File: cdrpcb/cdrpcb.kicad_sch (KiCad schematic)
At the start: 41 parts, among them J1 Conn_02x04_Odd_Even, J2 Conn_01x03, J3 Conn_01x03, J4 Conn_01x03, J5 Conn_01x03, J7 Conn_01x06, J8 Conn_01x04, J9 Conn_01x03, SW1 Conn_01x02_Pin, SW2 Conn_01x02_Pin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

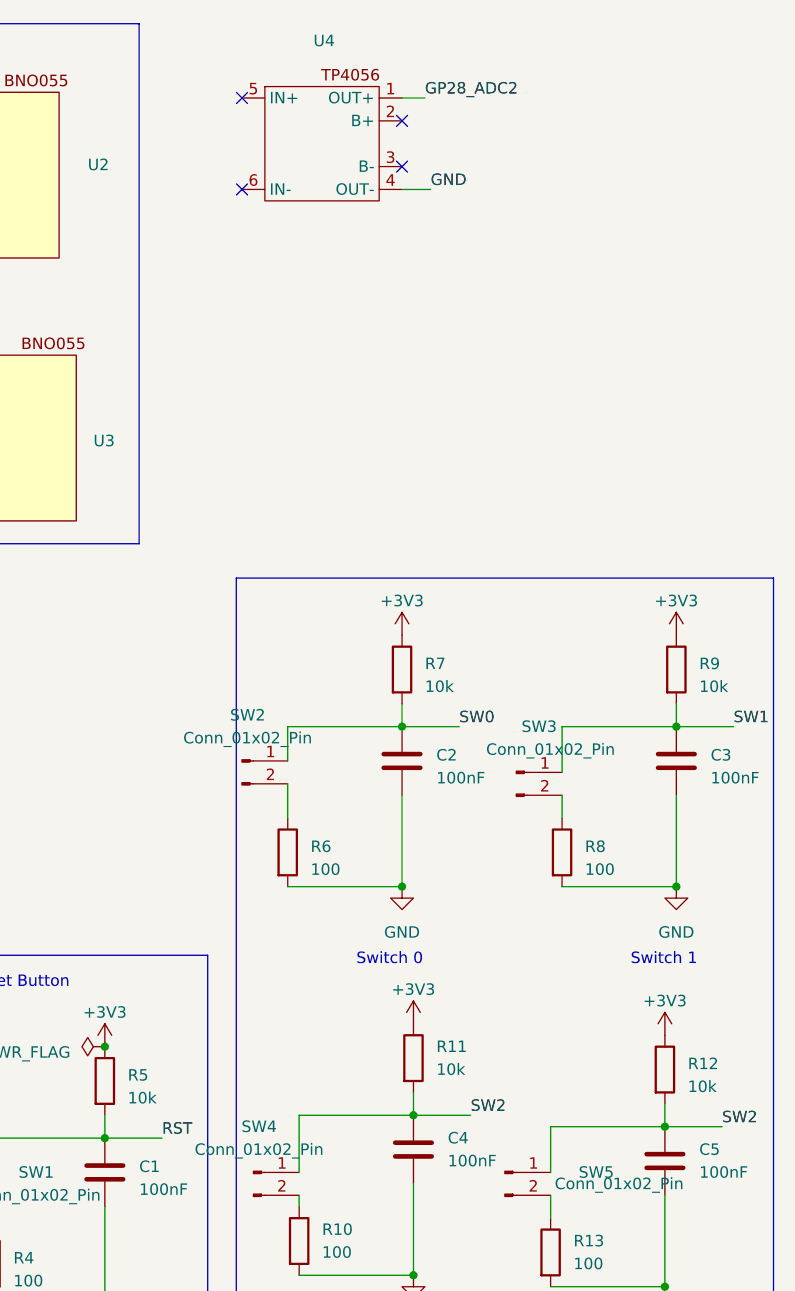
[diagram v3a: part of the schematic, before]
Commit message: add labels, fix charging circuit traces
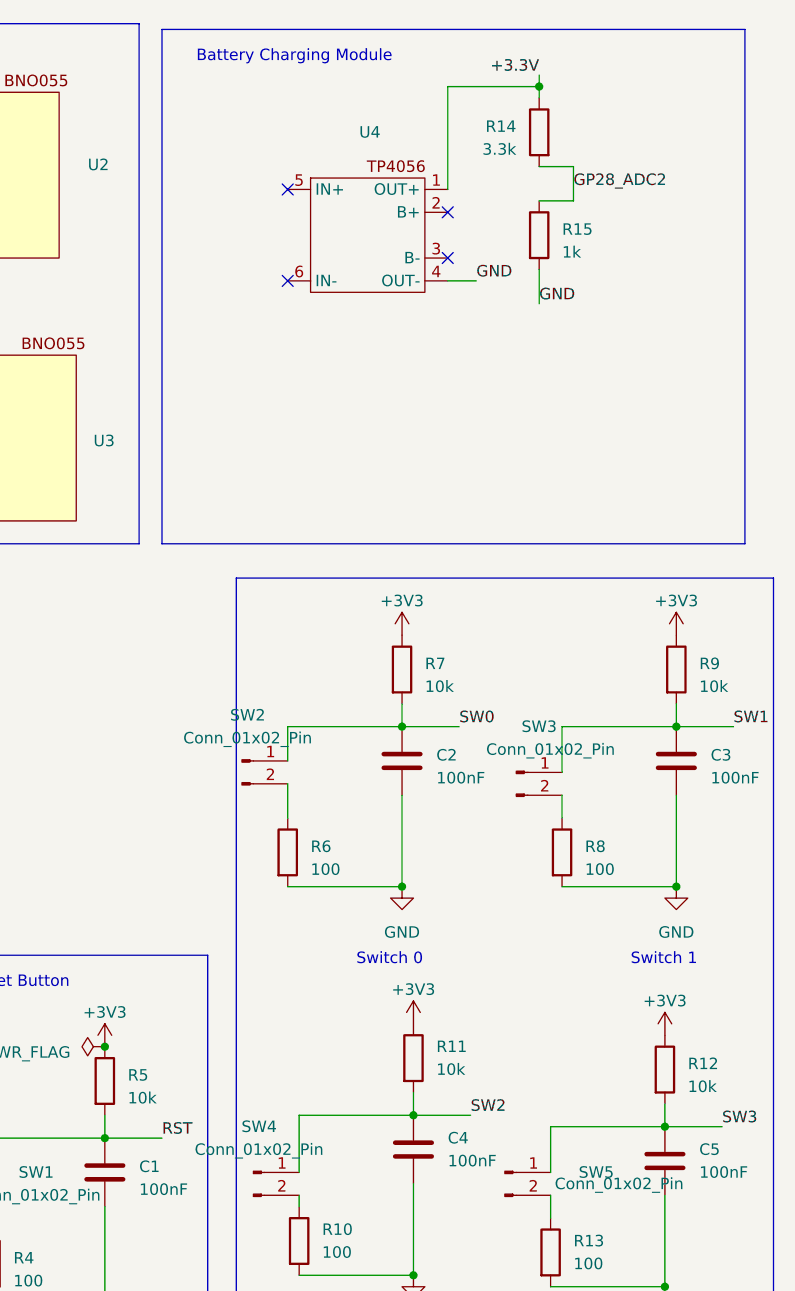
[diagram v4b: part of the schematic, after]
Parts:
- added R14: 3.3k, Resistor_THT:R_Axial_DIN0204_L3.6mm_D1.6mm_P1.90mm_Vertical, symbol Device:R
- added R15: 1k, Resistor_THT:R_Axial_DIN0204_L3.6mm_D1.6mm_P1.90mm_Vertical, symbol Device:R
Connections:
- net +3.3V: now also U4.1 (OUT+), R14.1
- net GND: now also R15.2
- net GP28_ADC2: now also R14.2, R15.1; no longer U4.1 (OUT+)
- net SW2: no longer C5.1, R12.2, SW5.1 (Pin_1)
- new net SW3: C5.1, R12.2, SW5.1 (Pin_1)
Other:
- note added: "Battery Charging Module"
- moved on the sheet: U4
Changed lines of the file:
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@@
   (junction (at 273.05 110.49) (diameter 0) (color 0 0 0 0)
   )
+  (junction (at 257.81 21.59) (diameter 0) (color 0 0 0 0)
+  )
   (no_connect (at 157.48 181.61))
-  (no_connect (at 242.57 30.48))
-  (no_connect (at 224.79 22.86))
+  (no_connect (at 247.65 40.64))
+  (no_connect (at 229.87 33.02))
   (no_connect (at 88.265 85.725))
-  (no_connect (at 242.57 25.4))
+  (no_connect (at 247.65 35.56))
   (no_connect (at 88.265 93.345))
   (no_connect (at 88.265 100.965))
   (no_connect (at 88.265 95.885))
-  (no_connect (at 224.79 33.02))
+  (no_connect (at 229.87 43.18))
   (no_connect (at 88.265 88.265))
   (no_connect (at 37.465 40.005))
@@
     (stroke (width 0) (type default))
   )
+  (wire (pts (xy 261.62 30.48) (xy 261.62 34.29))
+    (stroke (width 0) (type default))
+  )
   (wire (pts (xy 88.265 34.925) (xy 92.075 34.925))
     (stroke (width 0) (type default))
   )
-  (wire (pts (xy 242.57 33.02) (xy 245.745 33.02))
+  (wire (pts (xy 247.65 43.18) (xy 250.825 43.18))
     (stroke (width 0) (type default))
   )
@@
     (stroke (width 0) (type default))
   )
+  (wire (pts (xy 257.81 34.29) (xy 261.62 34.29))
+    (stroke (width 0) (type default))
+  )
   (wire (pts (xy 88.265 62.865) (xy 97.155 62.865))
     (stroke (width 0) (type default))
@@
     (stroke (width 0) (type default))
   )
-  (wire (pts (xy 242.57 22.86) (xy 245.11 22.86))
+  (wire (pts (xy 257.81 20.32) (xy 257.81 21.59))
     (stroke (width 0) (type default))
   )
@@
     (stroke (width 0) (type default))
   )
+  (wire (pts (xy 247.65 33.02) (xy 247.65 21.59))
+    (stroke (width 0) (type default))
+  )
   (wire (pts (xy 142.24 91.44) (xy 142.24 92.71))
     (stroke (width 0) (type default))
@@
     (stroke (width 0) (type default))
   )
+  (wire (pts (xy 247.65 21.59) (xy 257.81 21.59))
+    (stroke (width 0) (type default))
+  )
   (wire (pts (xy 31.115 57.785) (xy 37.465 57.785))
     (stroke (width 0) (type default))
@@
     (stroke (width 0) (type default))
   )
+  (wire (pts (xy 257.81 30.48) (xy 261.62 30.48))
+    (stroke (width 0) (type default))
+  )
   (wire (pts (xy 31.115 47.625) (xy 37.465 47.625))
     (stroke (width 0) (type default))
@@
     (stroke (width 0) (type default))
   )
+  (wire (pts (xy 257.81 21.59) (xy 257.81 22.86))
+    (stroke (width 0) (type default))
+  )
   (wire (pts (xy 89.535 112.395) (xy 92.075 112.395))
     (stroke (width 0) (type default))
@@
     (stroke (width 0) (type default))
   )
+  (wire (pts (xy 257.81 41.91) (xy 257.81 45.72))
+    (stroke (width 0) (type default))
+  )
   (wire (pts (xy 88.265 29.845) (xy 95.885 29.845))
     (stroke (width 0) (type default))
@@
   (wire (pts (xy 229.87 92.71) (xy 229.87 96.52))
     (stroke (width 0) (type default))
+  )
+  (rectangle (start 215.9 15.24) (end 280.67 72.39)
+    (stroke (width 0) (type default))
+    (fill (type none))
   )
   (text_box ""
@@
     (effects (font (size 1.27 1.27)) (justify left top))
   )
+  (text "Battery Charging Module" (at 219.71 19.05 0)
+    (effects (font (size 1.27 1.27)) (justify left bottom))
+  )
   (text "Switch 0" (at 237.49 119.38 0)
     (effects (font (size 1.27 1.27)) (justify left bottom))
@@
     (effects (font (size 1.27 1.27)) (justify right bottom))
   )
+  (label "GND" (at 257.81 45.72 0) (fields_autoplaced)
+    (effects (font (size 1.27 1.27)) (justify left bottom))
+  )
   (label "GP1_UART0_RX" (at 144.145 55.245 180) (fields_autoplaced)
     (effects (font (size 1.27 1.27)) (justify right bottom))
   )
-  (label "SW2" (at 278.13 137.16 0) (fields_autoplaced)
-    (effects (font (size 1.27 1.27)) (justify left bottom))
-  )
-  (label "GND" (at 245.745 33.02 0) (fields_autoplaced)
+  (label "SW3" (at 278.13 137.16 0) (fields_autoplaced)
+    (effects (font (size 1.27 1.27)) (justify left bottom))
+  )
+  (label "GND" (at 250.825 43.18 0) (fields_autoplaced)
     (effects (font (size 1.27 1.27)) (justify left bottom))
   )
@@
     (effects (font (size 1.27 1.27)) (justify right bottom))
   )
+  (label "+3.3V" (at 257.81 20.32 180) (fields_autoplaced)
+    (effects (font (size 1.27 1.27)) (justify right bottom))
+  )
   (label "SPI1_CS" (at 97.155 47.625 0) (fields_autoplaced)
     (effects (font (size 1.27 1.27)) (justify left bottom))
@@
     (effects (font (size 1.27 1.27)) (justify left bottom))
   )
-  (label "GP28_ADC2" (at 245.11 22.86 0) (fields_autoplaced)
+  (label "GP28_ADC2" (at 261.62 33.02 0) (fields_autoplaced)
     (effects (font (size 1.27 1.27)) (justify left bottom))
   )
@@
       (effects (font (size 1.27 1.27)) hide)
     )
-    (pin "2")
-    (pin "1")
+    (pin "1")
+    (pin "2")
     (instances
       (project "cdrpcb"
@@
     )
   )
-  (symbol (lib_id "TP4056:TP4056") (at 231.14 19.05 0) (unit 1)
-    (in_bom yes) (on_board yes) (dnp no) (fields_autoplaced)
-    (property "Reference" "U4" (at 233.917 16.51 0)
-      (effects (font (size 1.27 1.27)))
-    )
-    (property "Value" "~" (at 231.14 19.05 0)
-      (effects (font (size 1.27 1.27)))
-    )
-    (property "Footprint" "TP4056:TP4056-18650" (at 231.14 19.05 0)
-      (effects (font (size 1.27 1.27)) hide)
-    )
-    (property "Datasheet" "" (at 231.14 19.05 0)
-      (effects (font (size 1.27 1.27)) hide)
-    )
+  (symbol (lib_id "TP4056:TP4056") (at 236.22 29.21 0) (unit 1)
+    (in_bom yes) (on_board yes) (dnp no) (fields_autoplaced)
+    (property "Reference" "U4" (at 238.997 26.67 0)
+      (effects (font (size 1.27 1.27)))
+    )
+    (property "Value" "~" (at 236.22 29.21 0)
+      (effects (font (size 1.27 1.27)))
+    )
+    (property "Footprint" "TP4056:TP4056-18650" (at 236.22 29.21 0)
+      (effects (font (size 1.27 1.27)) hide)
+    )
+    (property "Datasheet" "" (at 236.22 29.21 0)
+      (effects (font (size 1.27 1.27)) hide)
+    )
+    (pin "1")
+    (pin "2")
     (pin "3")
     (pin "4")
-    (pin "2")
-    (pin "1")
     (pin "5")
     (pin "6")
@@
     )
   )
+  (symbol (lib_id "Device:R") (at 257.81 26.67 0) (mirror y) (unit 1)
+    (in_bom yes) (on_board yes) (dnp no)
+    (property "Reference" "R14" (at 255.27 26.035 0)
+      (effects (font (size 1.27 1.27)) (justify left))
+    )
+    (property "Value" "3.3k" (at 255.27 28.575 0)
+      (effects (font (size 1.27 1.27)) (justify left))
+    )
+    (property "Footprint" "Resistor_THT:R_Axial_DIN0204_L3.6mm_D1.6mm_P1.90mm_Vertical" (at 259.588 26.67 90)
+      (effects (font (size 1.27 1.27)) hide)
+    )
+    (property "Datasheet" "~" (at 257.81 26.67 0)
+      (effects (font (size 1.27 1.27)) hide)
+    )
+    (pin "1")
+    (pin "2")
+    (instances
+      (project "cdrpcb"
+        (path "/256b697e-9752-4e3a-a338-bc05701ab36e"
+          (reference "R14") (unit 1)
+        )
+      )
+    )
+  )
   (symbol (lib_id "power:GND") (at 92.075 108.585 90) (unit 1)
     (in_bom yes) (on_board yes) (dnp no) (fields_autoplaced)
@@
     )
     (pin "1")
+    (pin "2")
     (pin "3")
     (pin "4")
+    (pin "5")
     (pin "6")
-    (pin "5")
-    (pin "2")
     (instances
       (project "cdrpcb"
@@
     )
     (pin "1")
+    (pin "2")
     (pin "3")
     (pin "4")
+    (pin "5")
     (pin "6")
-    (pin "5")
-    (pin "2")
     (instances
       (project "cdrpcb"
@@
       (effects (font (size 1.27 1.27)) hide)
     )
-    (pin "2")
-    (pin "1")
+    (pin "1")
+    (pin "2")
     (instances
       (project "cdrpcb"
@@
         (path "/256b697e-9752-4e3a-a338-bc05701ab36e"
           (reference "#PWR08") (unit 1)
+        )
+      )
+    )
+  )
+  (symbol (lib_id "Device:R") (at 257.81 38.1 0) (unit 1)
+    (in_bom yes) (on_board yes) (dnp no) (fields_autoplaced)
+    (property "Reference" "R15" (at 260.35 37.465 0)
+      (effects (font (size 1.27 1.27)) (justify left))
+    )
+    (property "Value" "1k" (at 260.35 40.005 0)
+      (effects (font (size 1.27 1.27)) (justify left))
+    )
+    (property "Footprint" "Resistor_THT:R_Axial_DIN0204_L3.6mm_D1.6mm_P1.90mm_Vertical" (at 256.032 38.1 90)
+      (effects (font (size 1.27 1.27)) hide)
+    )
+    (property "Datasheet" "~" (at 257.81 38.1 0)
+      (effects (font (size 1.27 1.27)) hide)
+    )
+    (pin "1")
+    (pin "2")
+    (instances
+      (project "cdrpcb"
+        (path "/256b697e-9752-4e3a-a338-bc05701ab36e"
+          (reference "R15") (unit 1)
         )
       )
@@
       (effects (font (size 1.27 1.27)) hide)
     )
+    (pin "1")
+    (pin "2")
     (pin "3")
-    (pin "1")
-    (pin "8")
-    (pin "7")
+    (pin "4")
     (pin "5")
     (pin "6")
-    (pin "2")
-    (pin "4")
+    (pin "7")
+    (pin "8")
     (instances
       (project "cdrpcb"
@@
       (effects (font (size 1.27 1.27)) hide)
     )
-    (pin "2")
-    (pin "1")
+    (pin "1")
+    (pin "2")
     (instances
       (project "cdrpcb"
@@
       (effects (font (size 1.27 1.27) italic) hide)
     )
+    (pin "1")
+    (pin "2")
+    (pin "3")
+    (pin "4")
     (pin "5")
-    (pin "8")
-    (pin "1")
-    (pin "4")
     (pin "6")
     (pin "7")
-    (pin "3")
-    (pin "2")
+    (pin "8")
     (instances
       (project "cdrpcb"
@@
     )
     (pin "1")
+    (pin "2")
     (pin "3")
     (pin "4")
-    (pin "2")
-    (instances
-      (project "cdrpcb"
+    (instances
+      (project "cdrpcb"

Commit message: widened traces, fixed charging circuit (for real)
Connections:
- net +3.3V: no longer R14.1, U4.1 (OUT+)
- net +5V: now also R14.1, U4.1 (OUT+)
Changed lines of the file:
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@@
-    (effects (font (size 1.27 1.27)) (justify right bottom))
-  )
-  (label "+3.3V" (at 257.81 20.32 180) (fields_autoplaced)
     (effects (font (size 1.27 1.27)) (justify right bottom))
   )
@@
   )
   (symbol (lib_id "power:+5V") (at 95.885 29.845 270) (unit 1)
-    (in_bom yes) (on_board yes) (dnp no) (fields_autoplaced)
+    (in_bom yes) (on_board yes) (dnp no)
     (property "Reference" "#PWR05" (at 92.075 29.845 0)
       (effects (font (size 1.27 1.27)) hide)
     )
-    (property "Value" "+5V" (at 99.695 30.48 90)
+    (property "Value" "VSYS" (at 99.06 30.48 90)
       (effects (font (size 1.27 1.27)) (justify left))
     )
@@
       (effects (font (size 1.27 1.27)) hide)
     )
-    (property "Value" "+5V" (at 140.335 34.925 90)
+    (property "Value" "VSYS" (at 140.97 35.56 90)
       (effects (font (size 1.27 1.27)) (justify left))
     )
@@
         )
       )
+    )
+  )
+  (symbol (lib_id "power:+5V") (at 257.81 20.32 0) (unit 1)
+    (in_bom yes) (on_board yes) (dnp no)
+    (property "Reference" "#PWR032" (at 257.81 24.13 0)
+      (effects (font (size 1.27 1.27)) hide)
+    )
+    (property "Value" "VSYS" (at 258.445 17.145 0)
+      (effects (font (size 1.27 1.27)) (justify left))
+    )
+    (property "Footprint" "" (at 257.81 20.32 0)
+      (effects (font (size 1.27 1.27)) hide)
+    )
+    (property "Datasheet" "" (at 257.81 20.32 0)
+      (effects (font (size 1.27 1.27)) hide)
+    )
+    (pin "1")
+    (instances
+      (project "cdrpcb"
+        (path "/256b697e-9752-4e3a-a338-bc05701ab36e"
+          (reference "#PWR032") (unit 1)
+        )
+      )

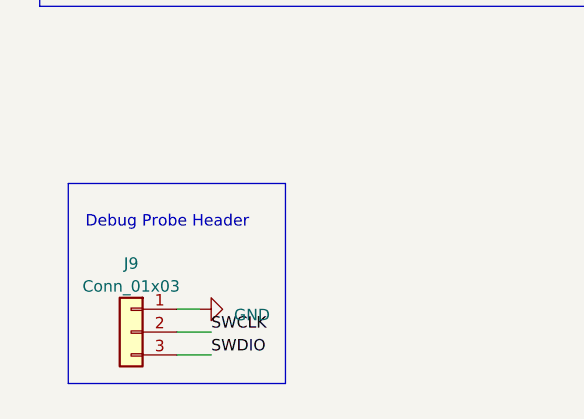
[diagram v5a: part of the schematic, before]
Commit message: fixing mounting hole distancing and spacing issues and also adding in custom 5.0mm footprint for holes in KiCad
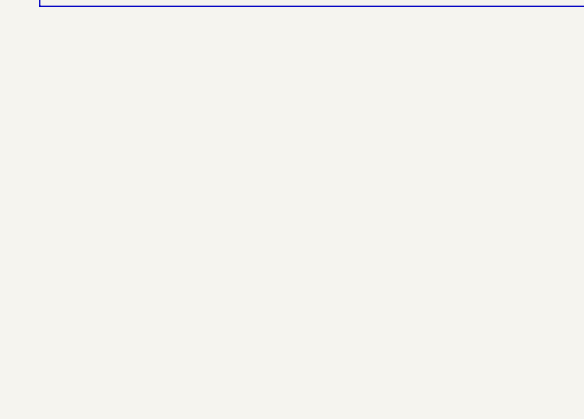
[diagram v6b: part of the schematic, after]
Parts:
- removed J9: Conn_01x03, Connector_PinHeader_2.54mm:PinHeader_1x03_P2.54mm_Vertical, symbol Connector_Generic:Conn_01x03
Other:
- note removed: "Debug Probe Header"
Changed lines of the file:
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@@
-    (stroke (width 0) (type default))
-  )
-  (wire (pts (xy 29.21 185.42) (xy 33.02 185.42))
     (stroke (width 0) (type default))
   )
@@
     (stroke (width 0) (type default))
   )
-  (wire (pts (xy 29.21 182.88) (xy 31.75 182.88))
-    (stroke (width 0) (type default))
-  )
   (wire (pts (xy 187.325 64.77) (xy 189.865 64.77))
     (stroke (width 0) (type default))
@@
   )
   (wire (pts (xy 231.14 153.67) (xy 243.84 153.67))
-    (stroke (width 0) (type default))
-  )
-  (wire (pts (xy 29.21 187.96) (xy 33.02 187.96))
     (stroke (width 0) (type default))
   )
@@
   )
   (text_box ""
-    (at 17.145 168.91 0) (size 24.13 22.225)
+    (at 126.365 14.605 0) (size 43.18 45.085)
     (stroke (width 0) (type default))
     (fill (type none))
@@
   )
   (text_box ""
-    (at 126.365 14.605 0) (size 43.18 45.085)
+    (at 125.095 66.04 0) (size 37.465 43.18)
     (stroke (width 0) (type default))
     (fill (type none))
@@
   )
   (text_box ""
-    (at 125.095 66.04 0) (size 37.465 43.18)
+    (at 189.23 118.11 0) (size 31.75 45.085)
     (stroke (width 0) (type default))
     (fill (type none))
@@
   )
   (text_box ""
-    (at 189.23 118.11 0) (size 31.75 45.085)
+    (at 13.97 13.97 0) (size 109.22 101.6)
     (stroke (width 0) (type default))
     (fill (type none))
@@
   )
   (text_box ""
-    (at 13.97 13.97 0) (size 109.22 101.6)
+    (at 13.97 119.38 0) (size 159.385 29.845)
     (stroke (width 0) (type default))
     (fill (type none))
@@
   )
   (text_box ""
-    (at 13.97 119.38 0) (size 159.385 29.845)
+    (at 224.155 76.2 0) (size 59.69 87.63)
     (stroke (width 0) (type default))
     (fill (type none))
@@
   )
   (text_box ""
-    (at 224.155 76.2 0) (size 59.69 87.63)
+    (at 167.005 93.98 0) (size 23.495 18.415)
     (stroke (width 0) (type default))
     (fill (type none))
     (effects (font (size 1.27 1.27)) (justify left top))
   )
-  (text_box ""
-    (at 167.005 93.98 0) (size 23.495 18.415)
+  (text_box "BNO055"
+    (at 174.625 14.605 0) (size 38.735 57.785)
     (stroke (width 0) (type default))
     (fill (type none))
     (effects (font (size 1.27 1.27)) (justify left top))
   )
-  (text_box "BNO055"
-    (at 174.625 14.605 0) (size 38.735 57.785)
-    (stroke (width 0) (type default))
-    (fill (type none))
-    (effects (font (size 1.27 1.27)) (justify left top))
-  )
   (text "Battery Charging Module" (at 219.71 19.05 0)
     (effects (font (size 1.27 1.27)) (justify left bottom))
@@
     (effects (font (size 1.27 1.27)) (justify left bottom))
   )
-  (text "Debug Probe Header" (at 19.05 173.99 0)
-    (effects (font (size 1.27 1.27)) (justify left bottom))
-  )
   (text "Switch 2" (at 238.76 162.56 0)
     (effects (font (size 1.27 1.27)) (justify left bottom))
@@
     (effects (font (size 1.27 1.27)) (justify right bottom))
   )
-  (label "SWDIO" (at 33.02 187.96 0) (fields_autoplaced)
-    (effects (font (size 1.27 1.27)) (justify left bottom))
-  )
   (label "SW0" (at 248.92 92.71 0) (fields_autoplaced)
     (effects (font (size 1.27 1.27)) (justify left bottom))
@@
   )
   (label "I2C1_SDA" (at 97.155 60.325 0) (fields_autoplaced)
-    (effects (font (size 1.27 1.27)) (justify left bottom))
-  )
-  (label "SWCLK" (at 33.02 185.42 0) (fields_autoplaced)
     (effects (font (size 1.27 1.27)) (justify left bottom))
   )
@@
     )
   )
-  (symbol (lib_id "Connector_Generic:Conn_01x03") (at 24.13 185.42 0) (mirror y) (unit 1)
-    (in_bom yes) (on_board yes) (dnp no) (fields_autoplaced)
-    (property "Reference" "J9" (at 24.13 177.8 0)
-      (effects (font (size 1.27 1.27)))
-    )
-    (property "Value" "Conn_01x03" (at 24.13 180.34 0)
-      (effects (font (size 1.27 1.27)))
-    )
-    (property "Footprint" "Connector_PinHeader_2.54mm:PinHeader_1x03_P2.54mm_Vertical" (at 24.13 185.42 0)
-      (effects (font (size 1.27 1.27)) hide)
-    )
-    (property "Datasheet" "~" (at 24.13 185.42 0)
-      (effects (font (size 1.27 1.27)) hide)
-    )
-    (pin "1")
-    (pin "2")
-    (pin "3")
-    (instances
-      (project "cdrpcb"
-        (path "/256b697e-9752-4e3a-a338-bc05701ab36e"
-          (reference "J9") (unit 1)
-        )
-      )
-    )
-  )
   (symbol (lib_id "power:VDDA") (at 67.31 134.62 90) (unit 1)
     (in_bom yes) (on_board yes) (dnp no)
@@
         )
       )
-    )
-  )
-  (symbol (lib_id "power:GND") (at 31.75 182.88 90) (unit 1)
-    (in_bom yes) (on_board yes) (dnp no) (fields_autoplaced)
-    (property "Reference" "#PWR049" (at 38.1 182.88 0)
-      (effects (font (size 1.27 1.27)) hide)
-    )
-    (property "Value" "GND" (at 35.56 183.515 90)
-      (effects (font (size 1.27 1.27)) (justify right))
-    )
-    (property "Footprint" "" (at 31.75 182.88 0)
-      (effects (font (size 1.27 1.27)) hide)
-    )
-    (property "Datasheet" "" (at 31.75 182.88 0)
-      (effects (font (size 1.27 1.27)) hide)
-    )
-    (pin "1")
-    (instances
-      (project "cdrpcb"
-        (path "/256b697e-9752-4e3a-a338-bc05701ab36e"
-          (reference "#PWR049") (unit 1)
-        )
-      )
